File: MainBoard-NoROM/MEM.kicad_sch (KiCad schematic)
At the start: 5 parts, among them U58 74ABT32, U59 74AHCT04

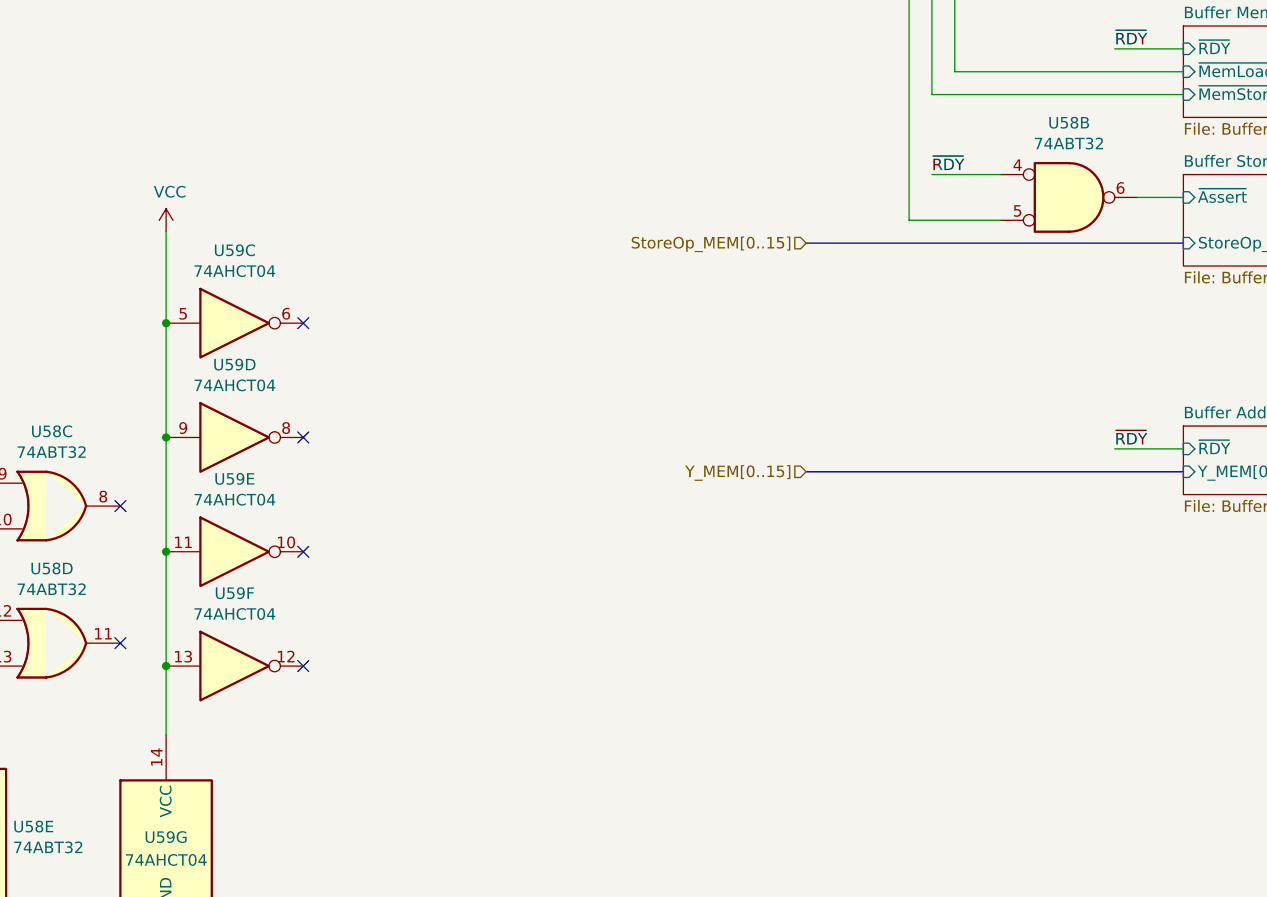
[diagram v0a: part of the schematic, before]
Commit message: MEMModule: Fix bug in the bank register reset signal
The bank register expects an active-high reset signal but was wired to
receive an active-low signal. Fix this issue by routing /RST_sync through
an inverter first.

BUG: The MainBoard PCB layout has not been updated yet.
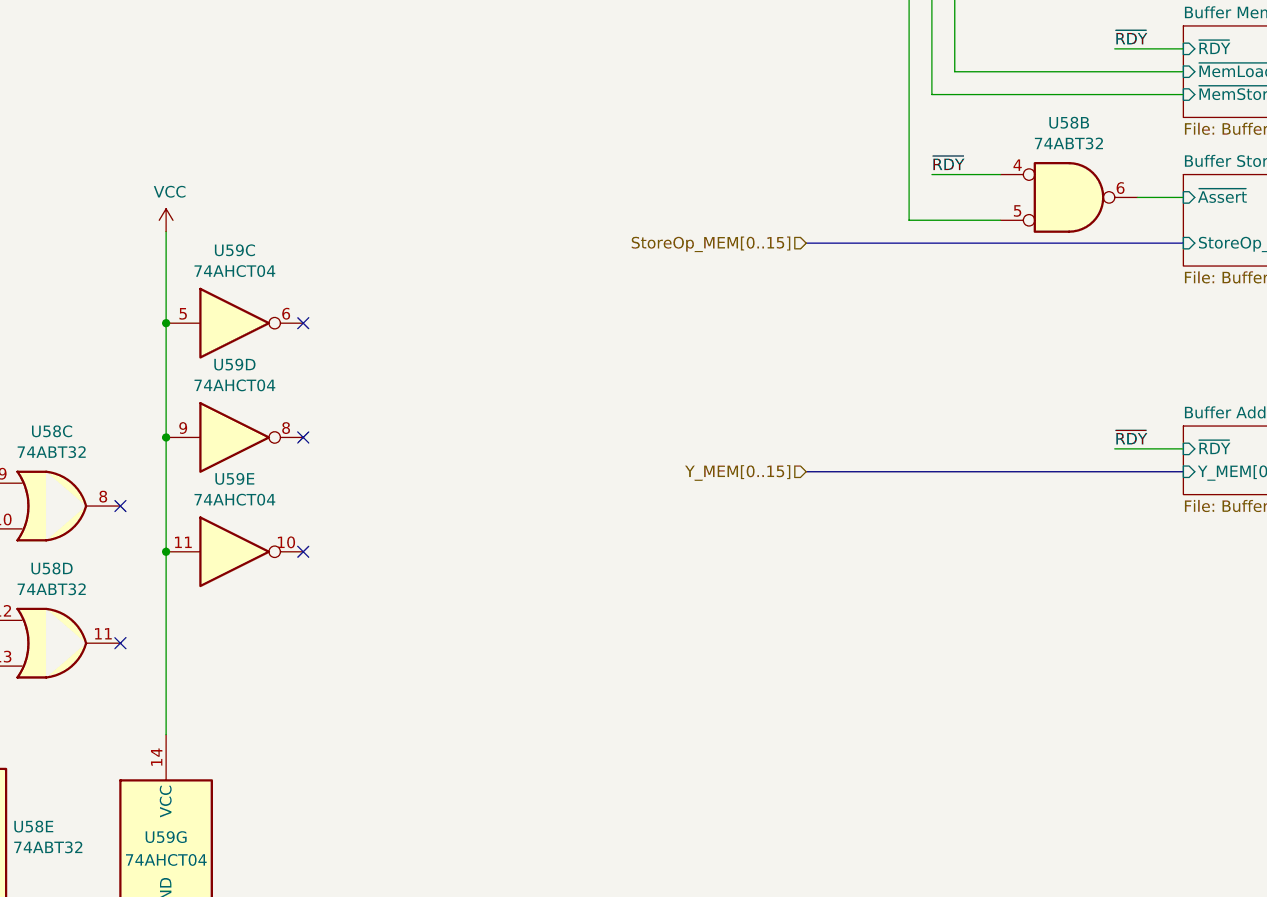
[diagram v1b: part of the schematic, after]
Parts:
- removed unit 6 of U59
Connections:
- no-connect marks 6 -> 5

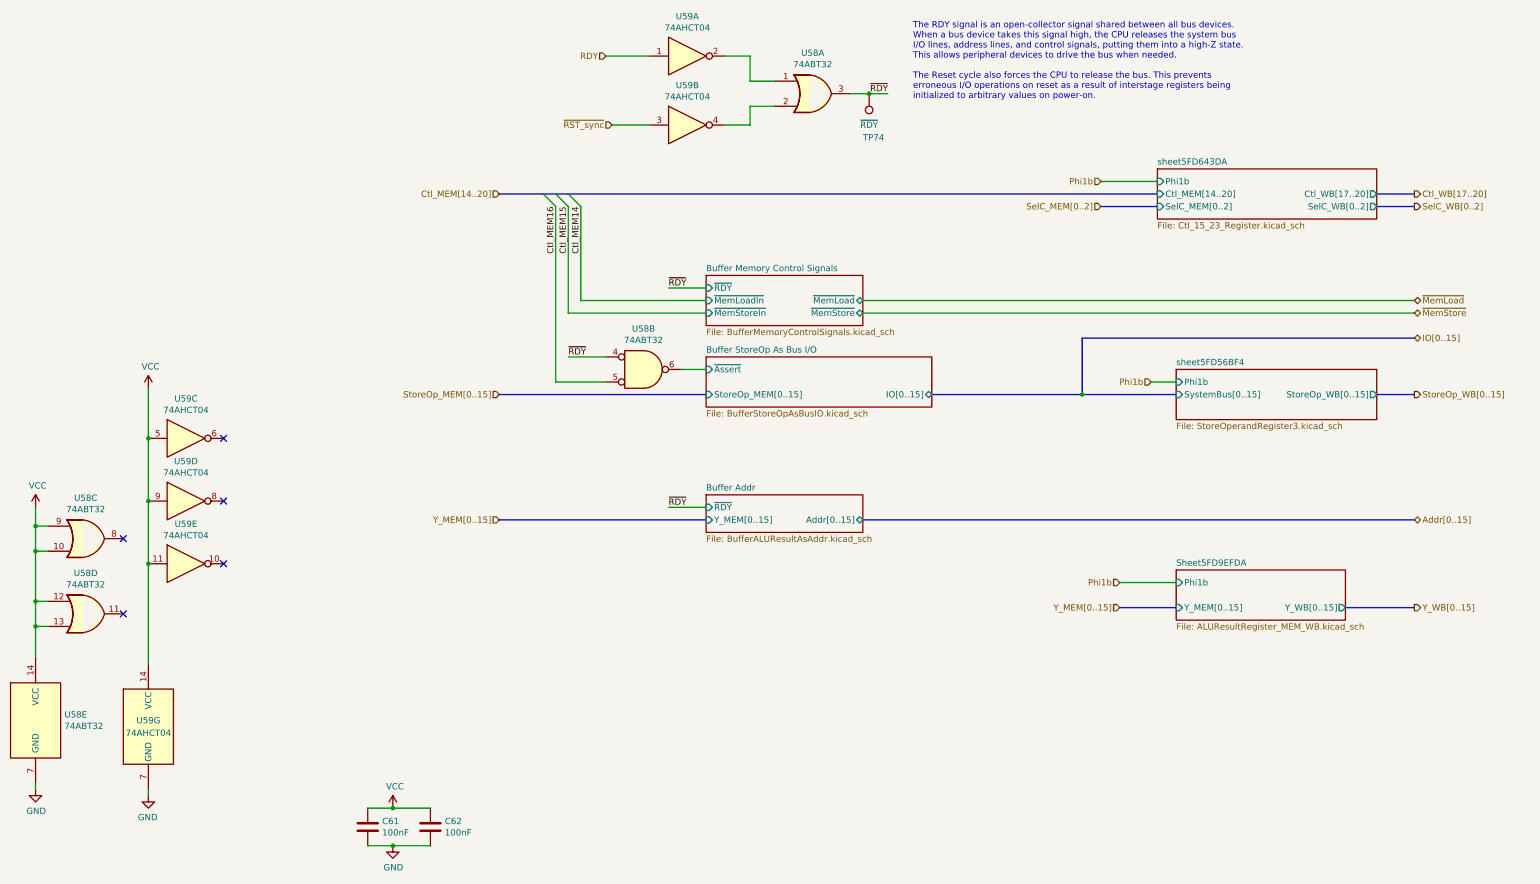
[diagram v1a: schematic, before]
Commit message: Update schematics for the MainBoard to include the ControleModule fix from 704c0dce
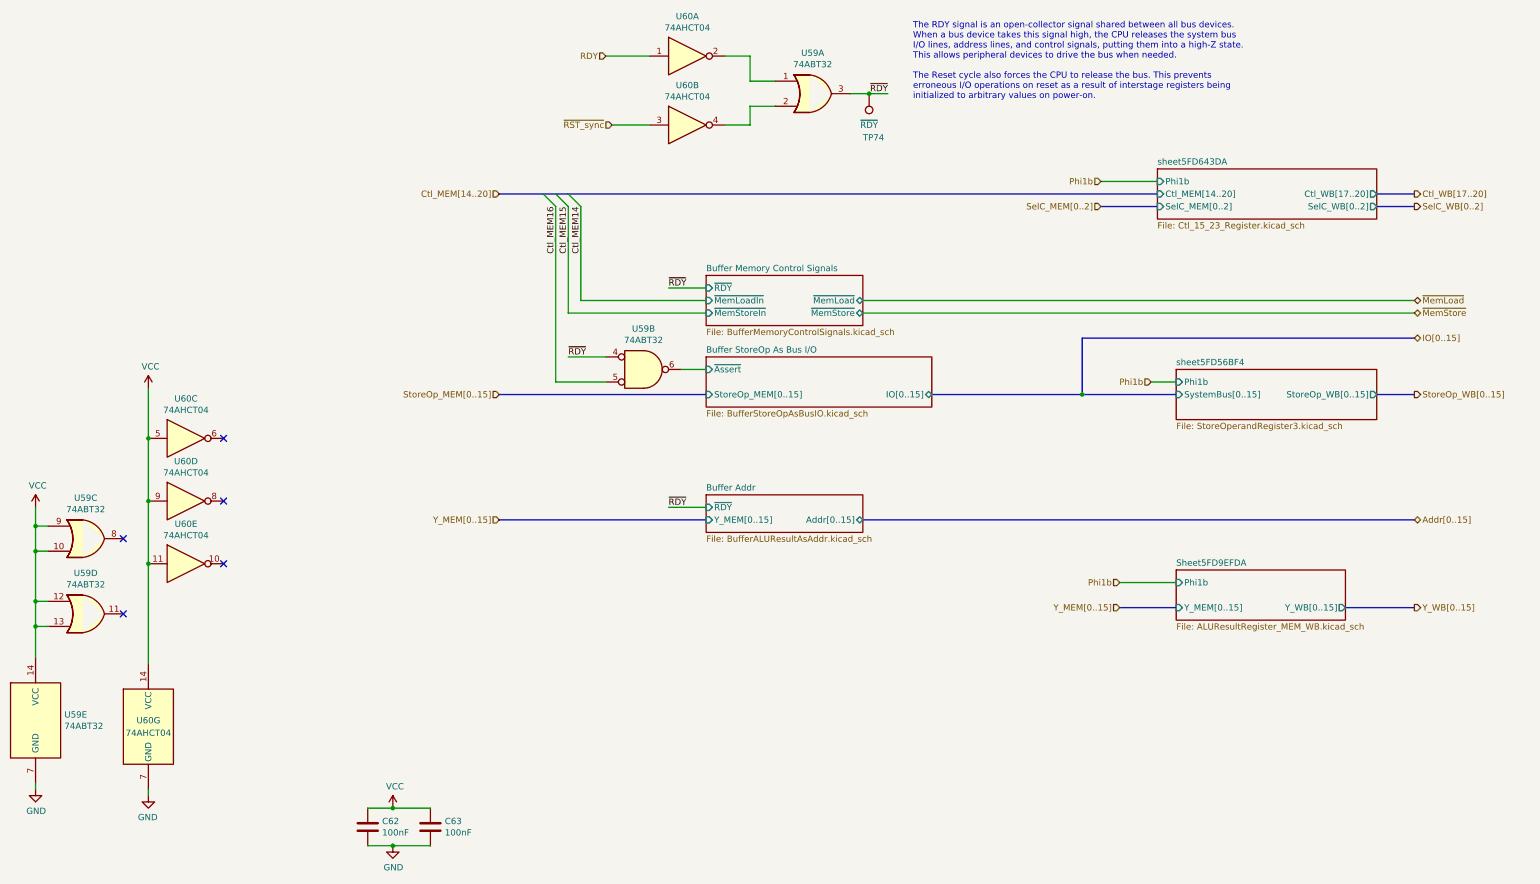
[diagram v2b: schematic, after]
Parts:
- renumbered C61 to C62, C62 to C63, U58 to U59, U59 to U60
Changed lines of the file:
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@@
   (symbol (lib_id "74xx:74LS04") (at 87.63 30.48 0) (unit 1)
     (in_bom yes) (on_board yes) (dnp no)
-    (property "Reference" "U59" (at 87.63 22.4282 0)
+    (property "Reference" "U60" (at 87.63 22.4282 0)
       (effects (font (size 1.27 1.27)))
     )
@@
       (project "MainBoard"
         (path "/83c5181e-f5ee-453c-ae5c-d7256ba8837d/00000000-0000-0000-0000-000060af64de"
-          (reference "U59") (unit 1)
+          (reference "U60") (unit 1)
         )
       )
@@
   (symbol (lib_id "74xx:74LS04") (at -21.59 166.37 0) (unit 7)
     (in_bom yes) (on_board yes) (dnp no)
-    (property "Reference" "U59" (at -21.59 165.1 0)
+    (property "Reference" "U60" (at -21.59 165.1 0)
       (effects (font (size 1.27 1.27)))
     )
@@
       (project "MainBoard"
         (path "/83c5181e-f5ee-453c-ae5c-d7256ba8837d/00000000-0000-0000-0000-000060af64de"
-          (reference "U59") (unit 7)
+          (reference "U60") (unit 7)
         )
       )
@@
   (symbol (lib_id "74xx:74LS04") (at -13.97 133.35 0) (unit 5)
     (in_bom yes) (on_board yes) (dnp no)
-    (property "Reference" "U59" (at -13.97 125.2982 0)
+    (property "Reference" "U60" (at -13.97 125.2982 0)
       (effects (font (size 1.27 1.27)))
     )
@@
       (project "MainBoard"
         (path "/83c5181e-f5ee-453c-ae5c-d7256ba8837d/00000000-0000-0000-0000-000060af64de"
-          (reference "U59") (unit 5)
+          (reference "U60") (unit 5)
         )
       )
@@
   (symbol (lib_id "74xx:74LS04") (at -13.97 120.65 0) (unit 4)
     (in_bom yes) (on_board yes) (dnp no)
-    (property "Reference" "U59" (at -13.97 112.5982 0)
+    (property "Reference" "U60" (at -13.97 112.5982 0)
       (effects (font (size 1.27 1.27)))
     )
@@
       (project "MainBoard"
         (path "/83c5181e-f5ee-453c-ae5c-d7256ba8837d/00000000-0000-0000-0000-000060af64de"
-          (reference "U59") (unit 4)
+          (reference "U60") (unit 4)
         )
       )
@@
   (symbol (lib_id "74xx:74LS04") (at -13.97 107.95 0) (unit 3)
     (in_bom yes) (on_board yes) (dnp no)
-    (property "Reference" "U59" (at -13.97 99.8982 0)
+    (property "Reference" "U60" (at -13.97 99.8982 0)
       (effects (font (size 1.27 1.27)))
     )
@@
       (project "MainBoard"
         (path "/83c5181e-f5ee-453c-ae5c-d7256ba8837d/00000000-0000-0000-0000-000060af64de"
-          (reference "U59") (unit 3)
+          (reference "U60") (unit 3)
         )
       )
@@
   (symbol (lib_id "power:VCC") (at -21.59 97.79 0) (unit 1)
     (in_bom yes) (on_board yes) (dnp no)
-    (property "Reference" "#PWR0316" (at -21.59 101.6 0)
+    (property "Reference" "#PWR0318" (at -21.59 101.6 0)
       (effects (font (size 1.27 1.27)) hide)
     )
@@
       (project "MainBoard"
         (path "/83c5181e-f5ee-453c-ae5c-d7256ba8837d/00000000-0000-0000-0000-000060af64de"
-          (reference "#PWR0316") (unit 1)
+          (reference "#PWR0318") (unit 1)
         )
       )
@@
   (symbol (lib_id "power:GND") (at -21.59 180.34 0) (mirror y) (unit 1)
     (in_bom yes) (on_board yes) (dnp no)
-    (property "Reference" "#PWR0317" (at -21.59 186.69 0)
+    (property "Reference" "#PWR0319" (at -21.59 186.69 0)
       (effects (font (size 1.27 1.27)) hide)
     )
@@
       (project "MainBoard"
         (path "/83c5181e-f5ee-453c-ae5c-d7256ba8837d/00000000-0000-0000-0000-000060af64de"
-          (reference "#PWR0317") (unit 1)
+          (reference "#PWR0319") (unit 1)
         )
       )
@@
   (symbol (lib_id "74xx:74LS04") (at 87.63 44.45 0) (unit 2)
     (in_bom yes) (on_board yes) (dnp no)
-    (property "Reference" "U59" (at 87.63 36.3982 0)
+    (property "Reference" "U60" (at 87.63 36.3982 0)
       (effects (font (size 1.27 1.27)))
     )
@@
       (project "MainBoard"
         (path "/83c5181e-f5ee-453c-ae5c-d7256ba8837d/00000000-0000-0000-0000-000060af64de"
-          (reference "U59") (unit 2)
+          (reference "U60") (unit 2)
         )
       )
@@
   (symbol (lib_id "power:GND") (at 27.94 190.5 0) (unit 1)
     (in_bom yes) (on_board yes) (dnp no)
-    (property "Reference" "#PWR0319" (at 27.94 196.85 0)
+    (property "Reference" "#PWR0321" (at 27.94 196.85 0)
       (effects (font (size 1.27 1.27)) hide)
     )
@@
       (project "MainBoard"
         (path "/83c5181e-f5ee-453c-ae5c-d7256ba8837d/00000000-0000-0000-0000-000060af64de"
-          (reference "#PWR0319") (unit 1)
+          (reference "#PWR0321") (unit 1)
         )
       )
@@
   (symbol (lib_id "power:VCC") (at 27.94 182.88 0) (unit 1)
     (in_bom yes) (on_board yes) (dnp no)
-    (property "Reference" "#PWR0318" (at 27.94 186.69 0)
+    (property "Reference" "#PWR0320" (at 27.94 186.69 0)
       (effects (font (size 1.27 1.27)) hide)
     )
@@
       (project "MainBoard"
         (path "/83c5181e-f5ee-453c-ae5c-d7256ba8837d/00000000-0000-0000-0000-000060af64de"
-          (reference "#PWR0318") (unit 1)
+          (reference "#PWR0320") (unit 1)
         )
       )
@@
   (symbol (lib_id "Device:C") (at 22.86 186.69 0) (unit 1)
     (in_bom yes) (on_board yes) (dnp no)
-    (property "Reference" "C61" (at 25.781 185.5216 0)
+    (property "Reference" "C62" (at 25.781 185.5216 0)
       (effects (font (size 1.27 1.27)) (justify left))
     )
@@
       (project "MainBoard"
         (path "/83c5181e-f5ee-453c-ae5c-d7256ba8837d/00000000-0000-0000-0000-000060af64de"
-          (reference "C61") (unit 1)
+          (reference "C62") (unit 1)
         )
       )
@@
   (symbol (lib_id "power:VCC") (at -44.45 121.92 0) (unit 1)
     (in_bom yes) (on_board yes) (dnp no)
-    (property "Reference" "#PWR0314" (at -44.45 125.73 0)
+    (property "Reference" "#PWR0316" (at -44.45 125.73 0)
       (effects (font (size 1.27 1.27)) hide)
     )
@@
       (project "MainBoard"
         (path "/83c5181e-f5ee-453c-ae5c-d7256ba8837d/00000000-0000-0000-0000-000060af64de"
-          (reference "#PWR0314") (unit 1)
+          (reference "#PWR0316") (unit 1)
         )
       )
@@
   (symbol (lib_id "power:GND") (at -44.45 179.07 0) (unit 1)
     (in_bom yes) (on_board yes) (dnp no)
-    (property "Reference" "#PWR0315" (at -44.45 185.42 0)
+    (property "Reference" "#PWR0317" (at -44.45 185.42 0)
       (effects (font (size 1.27 1.27)) hide)
     )
@@
       (project "MainBoard"
         (path "/83c5181e-f5ee-453c-ae5c-d7256ba8837d/00000000-0000-0000-0000-000060af64de"
-          (reference "#PWR0315") (unit 1)
+          (reference "#PWR0317") (unit 1)
         )
       )
@@
   (symbol (lib_id "74xx:74LS32") (at 78.74 93.98 0) (unit 2) (convert 2)
     (in_bom yes) (on_board yes) (dnp no)
-    (property "Reference" "U58" (at 78.74 85.725 0)
+    (property "Reference" "U59" (at 78.74 85.725 0)
       (effects (font (size 1.27 1.27)))
     )
@@
       (project "MainBoard"
         (path "/83c5181e-f5ee-453c-ae5c-d7256ba8837d/00000000-0000-0000-0000-000060af64de"
-          (reference "U58") (unit 2)
+          (reference "U59") (unit 2)
         )
       )
@@
   (symbol (lib_id "74xx:74LS32") (at -34.29 128.27 0) (unit 3)
     (in_bom yes) (on_board yes) (dnp no)
-    (property "Reference" "U58" (at -34.29 120.015 0)
+    (property "Reference" "U59" (at -34.29 120.015 0)
       (effects (font (size 1.27 1.27)))
     )
@@
       (project "MainBoard"
         (path "/83c5181e-f5ee-453c-ae5c-d7256ba8837d/00000000-0000-0000-0000-000060af64de"
-          (reference "U58") (unit 3)
+          (reference "U59") (unit 3)
         )
       )
@@
   (symbol (lib_id "74xx:74LS32") (at -34.29 143.51 0) (unit 4)
     (in_bom yes) (on_board yes) (dnp no)
-    (property "Reference" "U58" (at -34.29 135.255 0)
+    (property "Reference" "U59" (at -34.29 135.255 0)
       (effects (font (size 1.27 1.27)))
     )
@@
       (project "MainBoard"
         (path "/83c5181e-f5ee-453c-ae5c-d7256ba8837d/00000000-0000-0000-0000-000060af64de"
-          (reference "U58") (unit 4)
+          (reference "U59") (unit 4)
         )
       )
@@
   (symbol (lib_id "74xx:74LS32") (at -44.45 165.1 0) (unit 5)
     (in_bom yes) (on_board yes) (dnp no)
-    (property "Reference" "U58" (at -38.608 163.9316 0)
+    (property "Reference" "U59" (at -38.608 163.9316 0)
       (effects (font (size 1.27 1.27)) (justify left))
     )
@@
       (project "MainBoard"
         (path "/83c5181e-f5ee-453c-ae5c-d7256ba8837d/00000000-0000-0000-0000-000060af64de"
-          (reference "U58") (unit 5)
+          (reference "U59") (unit 5)
         )
       )
@@
   (symbol (lib_id "74xx:74LS32") (at 113.03 38.1 0) (unit 1)
     (in_bom yes) (on_board yes) (dnp no)
-    (property "Reference" "U58" (at 113.03 29.845 0)
+    (property "Reference" "U59" (at 113.03 29.845 0)
       (effects (font (size 1.27 1.27)))
     )
@@
       (project "MainBoard"
         (path "/83c5181e-f5ee-453c-ae5c-d7256ba8837d/00000000-0000-0000-0000-000060af64de"
-          (reference "U58") (unit 1)
+          (reference "U59") (unit 1)
         )
       )
@@
   (symbol (lib_id "Device:C") (at 35.56 186.69 0) (unit 1)
     (in_bom yes) (on_board yes) (dnp no)
-    (property "Reference" "C62" (at 38.481 185.5216 0)
+    (property "Reference" "C63" (at 38.481 185.5216 0)
       (effects (font (size 1.27 1.27)) (justify left))
     )
@@
       (project "MainBoard"
         (path "/83c5181e-f5ee-453c-ae5c-d7256ba8837d/00000000-0000-0000-0000-000060af64de"
-          (reference "C62") (unit 1)
-        )
-      )
+          (reference "C63") (unit 1)
+        )
+      )
